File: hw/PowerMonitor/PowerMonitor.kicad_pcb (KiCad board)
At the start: 4 copper layers, 100 x 100 mm, 157 parts, among them J1 Conn_01x02_Socket, J2 Conn_01x02_Socket, J3 Conn_01x02_Socket, J4 Conn_01x02_Socket, J5 Conn_01x02_Socket, K1 Relay_SPST-NO, Q1 AO3400A, Q10 AO3400A, Q11 AO3400A, Q12 AO3400A, Q13 AO3400A, Q14 X0202MN, Q15 Q_PMOS_GDS, Q16 AO3400A, Q17 AO3400A, Q18 AO3400A, Q19 Q_PMOS_GDS, Q2 AO3400A, Q20 AO3400A, Q3 Q_PMOS_GDS, Q4 AO3400A, Q5 AO3400A, Q6 AO3400A, Q7 AO3400A, Q8 AO3400A, Q9 AO3400A, SW1 SW_Wuerth_450301014042, U1 LM393, U2 LM358, U3 LM393, U4 INA129, U5 LM358, U6 LM393, U7 LM393, U8 LM358

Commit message: powmon: more thermal considerations
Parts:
- moved TP26 11.0 mm to (164.0, 58.2)
- moved TP27 9.90 mm to (160.0, 58.2)
- moved TP7 4.30 mm to (169.5, 48.0)
- moved TP25 2.25 mm to (111.0, 117.2)
- moved D3 2.02 mm to (100.2, 76.8)
- moved D4 1.75 mm to (100.2, 70.5)
- moved D1 1.10 mm to (126.2, 46.4)
- moved D2 1.10 mm to (130.0, 46.4)
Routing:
- net /CellMonitor2/Vprot: track 208.8 -> 146.2 mm, vias 60 -> 111
- net +10V: track 127.0 -> 144.9 mm, vias 61 -> 64
- net /CellMonitor3/Vprot: track 21.3 -> 16.2 mm, vias 55 -> 59
- net GND: track 86.6 -> 84.1 mm, vias 89 -> 117
- net /VDIST: track 2.25 -> 0.00 mm, vias 36 -> 245
- net Net-(D1-K): track 58.2 -> 56.0 mm
- net /CellMonitor2/VbatH: track 33.4 -> 34.8 mm, vias 61 -> 53
- net Net-(D6-K): track 71.2 -> 69.9 mm
- net Net-(R3-Pad1): track 11.6 -> 12.6 mm
- net Net-(D3-K): track 38.4 -> 37.5 mm, vias 2 -> 3
- net Net-(D2-K): track 45.1 -> 44.6 mm
- net /CellMonitor1/VbatH: track 21.3 -> 21.6 mm, vias 76 -> 96
- net /CellMonitor1/Vprot: track 132.3 -> 132.0 mm, vias 104 -> 124
- net VDC: vias 30 -> 50
- added copper zone on B.Cu, net /CellMonitor2/Vprot

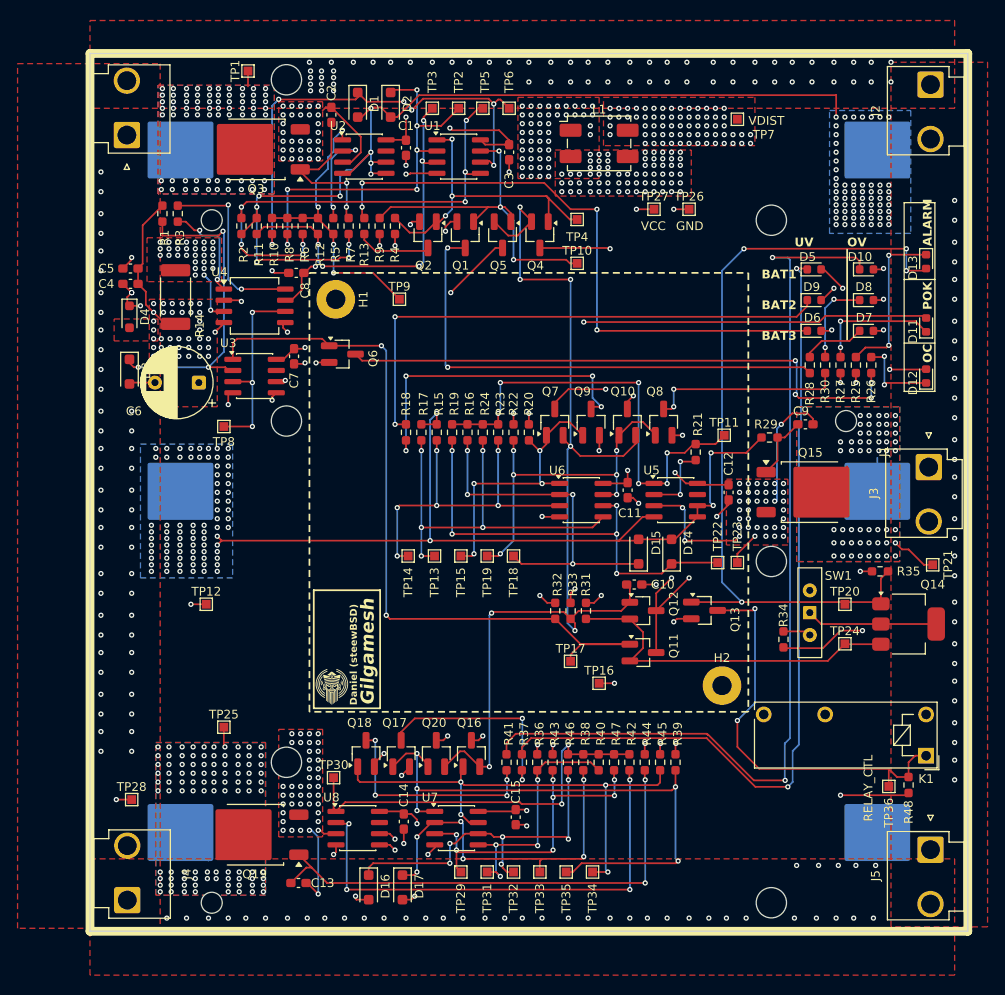
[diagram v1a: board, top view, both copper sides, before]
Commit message: powmon: update to kicad 10
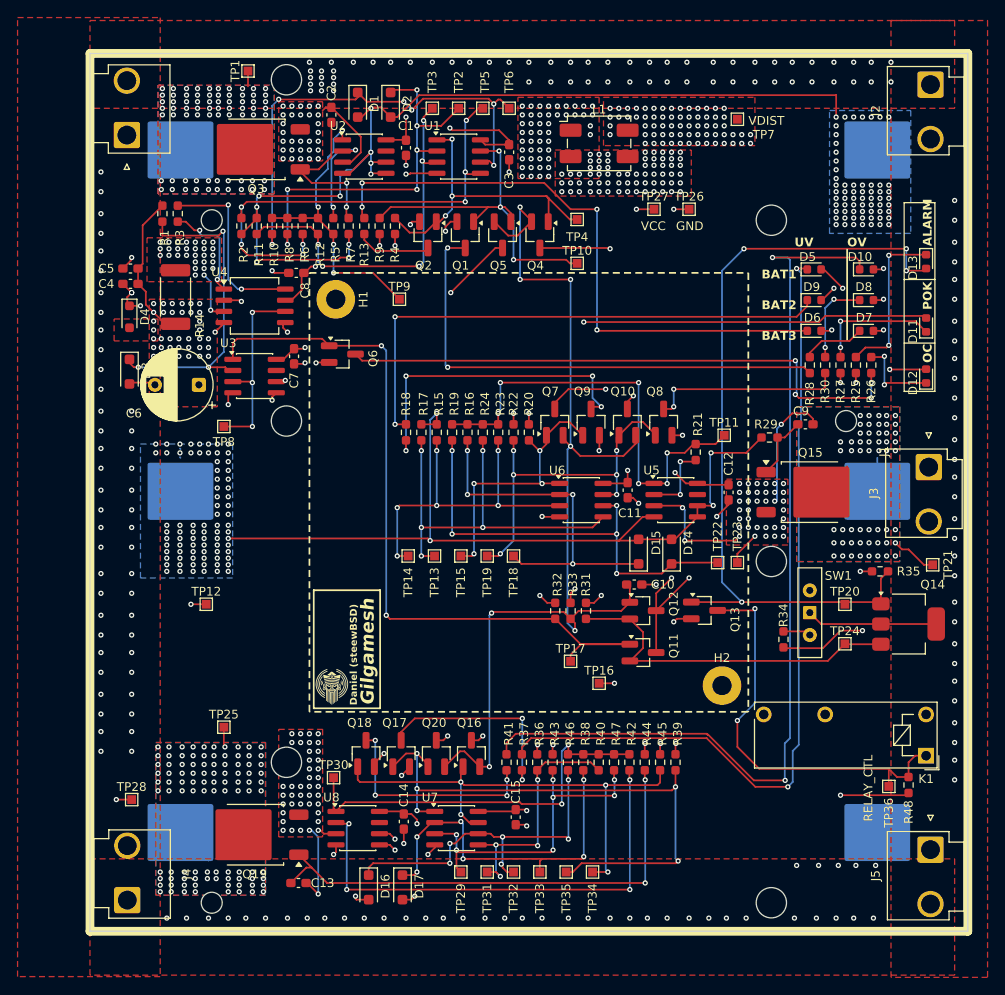
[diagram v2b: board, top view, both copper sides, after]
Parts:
- moved C6 0.25 mm to (108.2, 78.2)
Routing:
- net /CellMonitor1/Vprot: track 132.0 -> 130.0 mm

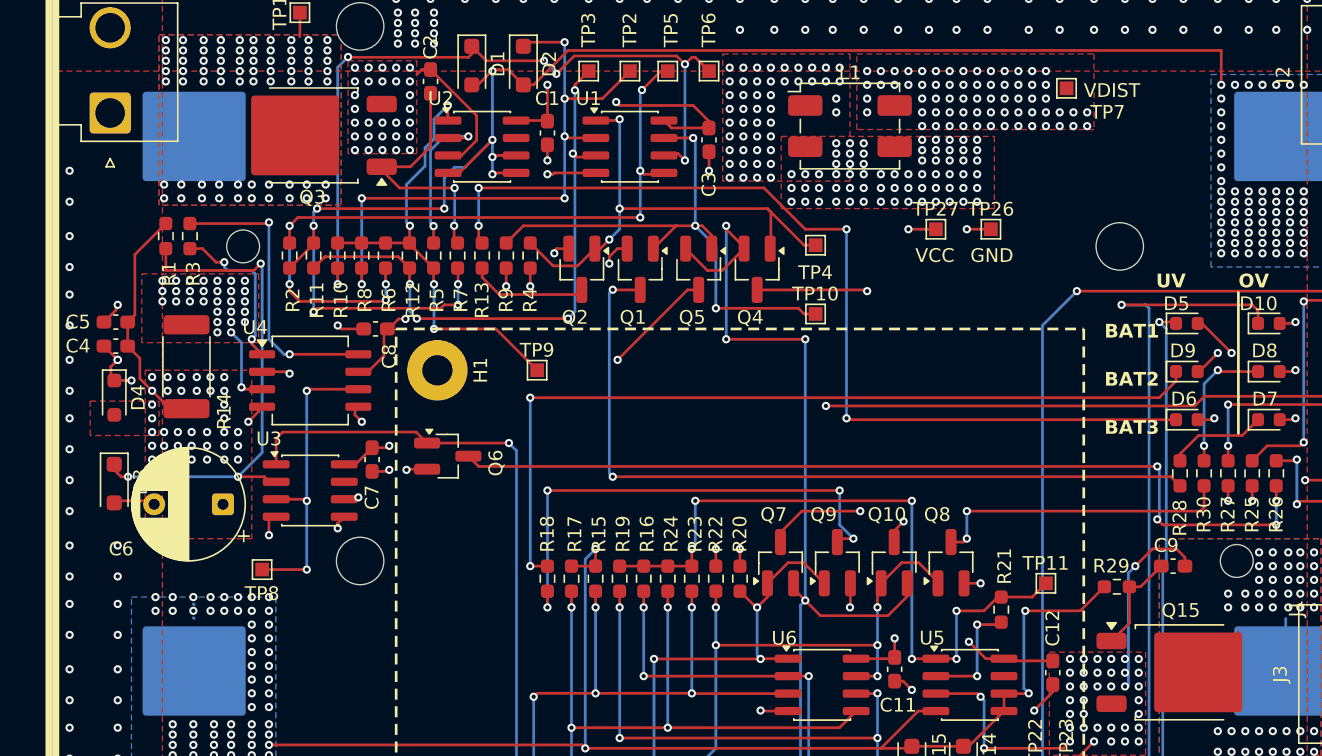
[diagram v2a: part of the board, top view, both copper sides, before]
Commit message: remote_ctrl: start working on it
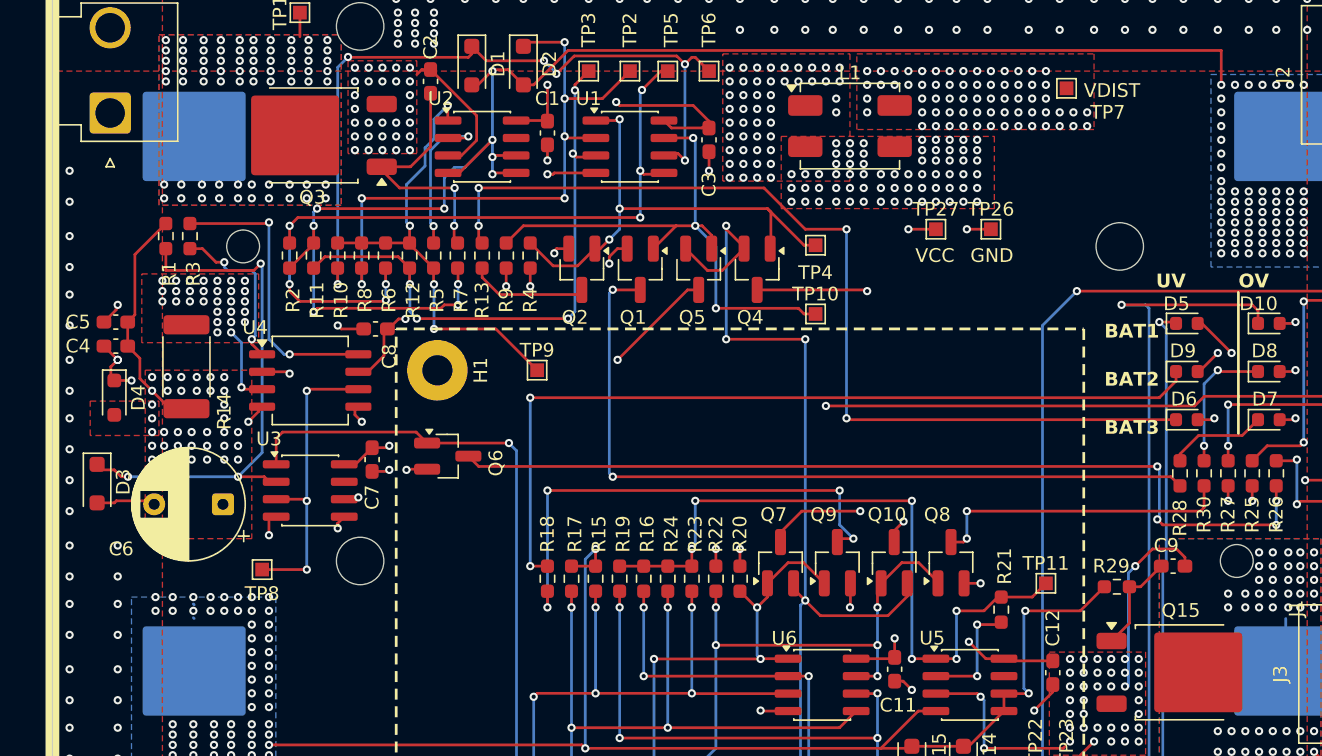
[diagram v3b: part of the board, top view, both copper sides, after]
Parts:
- moved D3 1.25 mm to (99.0, 76.8)
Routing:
- net /CellMonitor2/VbatH: track 34.8 -> 18.5 mm
- net GND: track 84.2 -> 85.4 mm
- net Net-(D3-K): track 37.5 -> 38.5 mm
